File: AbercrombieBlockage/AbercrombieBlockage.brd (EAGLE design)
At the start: 56 x 51 mm, 30 parts, among them U1 CY8CKIT-142, U2 DMN3135LVT, U3 DMN3135LVT, U4 DMN3135LVT, U5 M95M01, U6 LDK130M-R

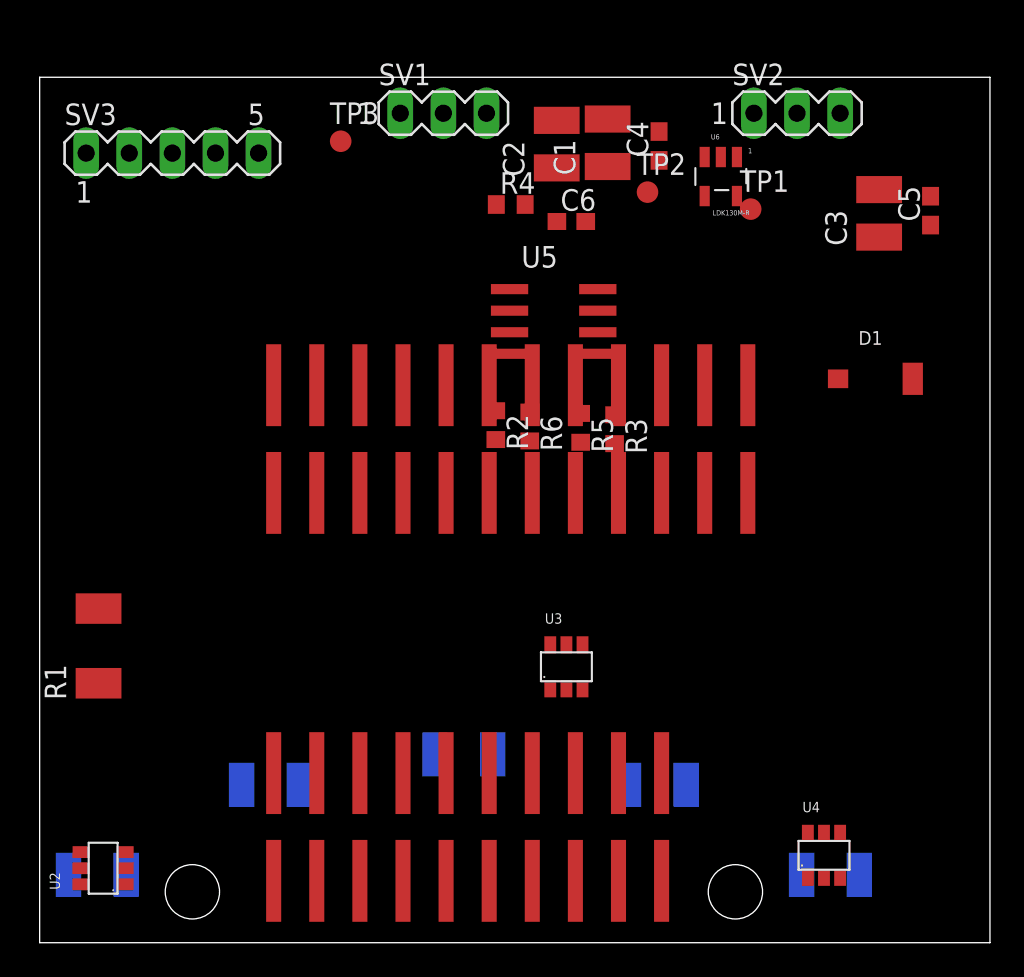
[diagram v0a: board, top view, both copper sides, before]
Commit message: Finished the schematic and placement. Starting routing for Abercrombie.
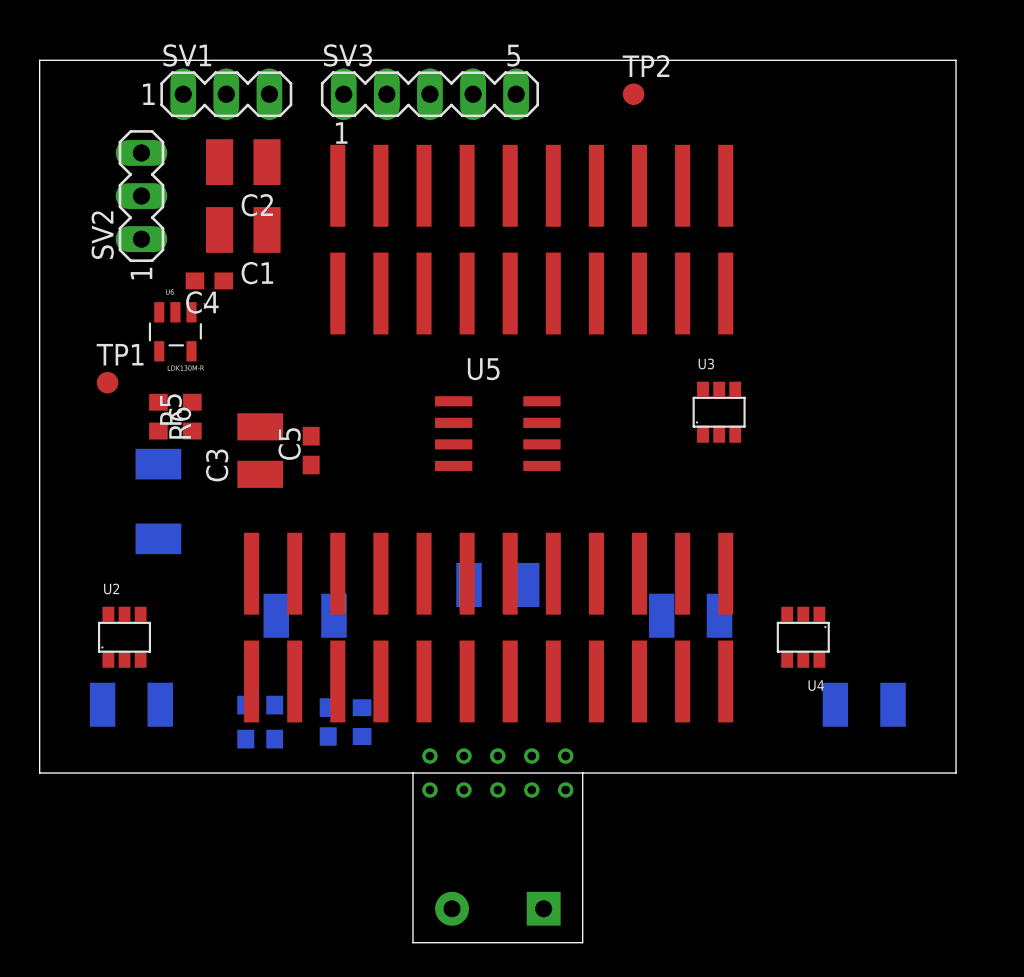
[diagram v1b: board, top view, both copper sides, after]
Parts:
- removed TP3: TPB1,27, testpad:B1,27
- D1: value BPW34 -> BPW34TH; device NicksParts:BPW34S -> NicksParts:BPW34
- moved TP1 39.3 mm to (4.00, 33.0)
- moved C5 39.1 mm to (16.0, 29.0)
- moved C3 39.1 mm to (13.0, 29.0)
- moved SV2 38.9 mm to (6.00, 44.0), turned to 90 degrees
- moved D1 38.3 mm to (27.0, 2.00), flipped to the bottom
- moved R4 34.8 mm to (13.0, 12.0), flipped to the bottom, turned to 180 degrees
- moved U6 33.4 mm to (8.00, 36.0)
- moved C6 32.8 mm to (17.0, 13.0), flipped to the bottom, turned to 90 degrees
- moved C4 27.7 mm to (10.0, 39.0), turned to 180 degrees
- moved R3 26.5 mm to (13.0, 14.0), flipped to the bottom, turned to 0 degrees
- moved R5 22.9 mm to (9.00, 31.0), turned to 90 degrees
- moved C1 22.1 mm to (12.0, 42.0), turned to 180 degrees
- moved R6 21.9 mm to (7.00, 31.0)
- moved R2 19.2 mm to (19.0, 13.0), flipped to the bottom
- moved C2 18.5 mm to (12.0, 46.0), turned to 180 degrees
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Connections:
- removed net N$11: C6.1, D1.C, R2.2, U1.P2.1
- removed net N$13: R3.2, R4.1, U1.P2.0
- removed net N$9: C6.2, R2.1, U1.P2.2
- new net OPAMP+: R3.2, R4.1, U1.2.0
- new net OPAMP-: C6.1, D1.C, R2.2, U1.2.1
- new net OPAMP_OUT: C6.2, R2.1, U1.2.2
- net CS: now also U1.1.5; no longer U1.P1.5
- net GND: now also U1.GND1
- net HOLD: now also U1.0.4; no longer U1.P0.4
- net LED1: now also U1.5.0; no longer U1.P3.6
- net LED2: now also U1.5.1; no longer U1.P3.4
- net LED3: now also U1.3.1; no longer U1.P3.2
- net LED4: now also U1.3.3; no longer U1.P3.0
- net LED5: now also U1.3.5; no longer U1.P4.0
- net MISO: now also U1.1.7; no longer U1.P1.6
- net MOSI: now also U1.0.0; no longer U1.P1.7
- net SCLK: now also U1.0.2; no longer U1.P1.3
- net SWDCLK: now also U1.0.7; no longer U1.P0.7
- net SWDIO: now also U1.0.6; no longer U1.P0.6
- net VREF: no longer U1.VREF
- net WP: now also U1.1.6; no longer U1.P1.4
- net XRES: no longer TP3.TP
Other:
- board size 56 x 51 mm -> 54 x 52 mm

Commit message: Fully routed Abercrombie design
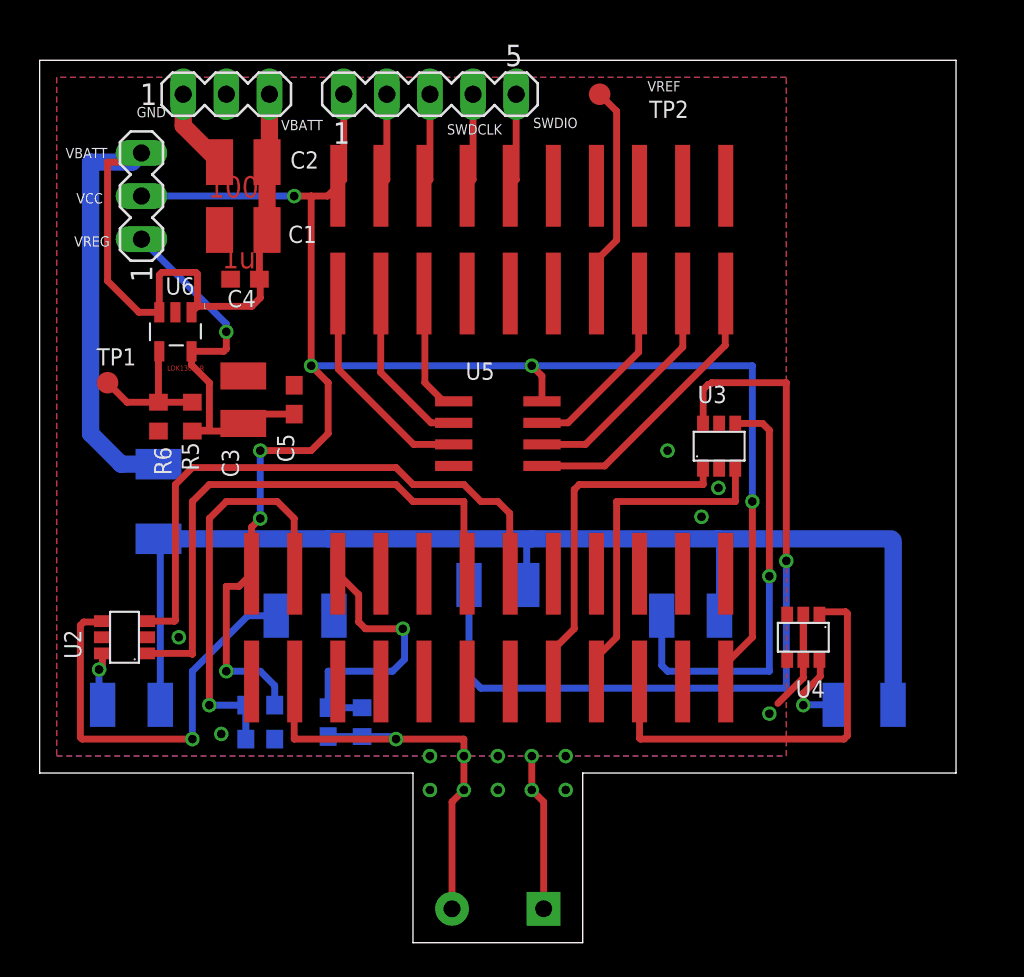
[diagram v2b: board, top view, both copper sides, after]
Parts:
- moved C3 3.16 mm to (12.0, 32.0)
- moved C5 3.16 mm to (15.0, 32.0)
- moved C4 2.10 mm to (12.1, 39.1)
- moved TP2 2.00 mm to (33.0, 50.0)
- moved U3 2.00 mm to (40.0, 29.3)
- turned U2 to 90 degrees
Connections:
- removed net VREF: TP2.TP
- new net N$9: TP2.TP, U1.VREF
- net LED1: now also U1.4.1; no longer U1.5.0
- net LED2: now also U1.4.0; no longer U1.5.1
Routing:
- net VCC: track 0.00 -> 102.4 mm, vias 0 -> 7
- net N$1: track 0.00 -> 74.9 mm
- net VBATT: track 0.00 -> 60.1 mm
- net N$4: track 0.00 -> 49.5 mm, vias 0 -> 1
- net LED2: track 0.00 -> 34.5 mm
- net LED1: track 0.00 -> 32.9 mm
- net GND: track 0.00 -> 28.1 mm, vias 0 -> 7
- net OPAMP-: track 0.00 -> 27.8 mm, vias 0 -> 1
- net N$5: track 0.00 -> 25.8 mm, vias 0 -> 1
- net N$3: track 0.00 -> 24.9 mm, vias 0 -> 1
- net LED5: track 0.00 -> 24.7 mm
- net OPAMP+: track 0.00 -> 24.2 mm, vias 0 -> 1
- net N$7: track 0.00 -> 23.2 mm, vias 0 -> 1
- net LED3: track 0.00 -> 20.5 mm
- net LED4: track 0.00 -> 20.1 mm
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- added copper zone on layer 1, net GND
- added copper zone on layer 16, net GND
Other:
- board text added: "GND"
- board text added: "SWDCLK"
- board text added: "SWDIO"
- board text added: "VBATT"
- board text added: "VCC"
- board text added: "VREF"
- board text added: "VREG"

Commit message: Minor update to the BLE connector
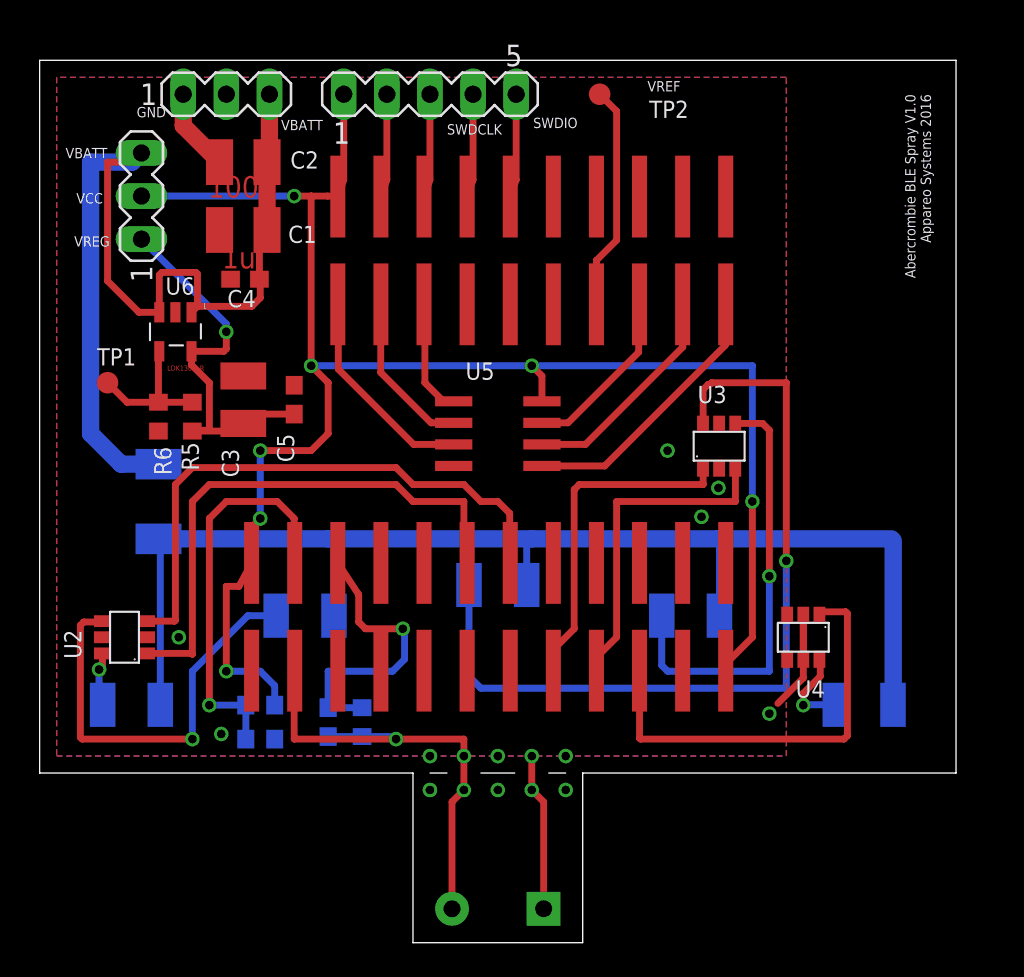
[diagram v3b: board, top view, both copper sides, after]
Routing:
- net N$9: track 12.7 -> 13.3 mm
- net LED5: track 24.7 -> 25.3 mm
- net LED3: track 20.5 -> 19.9 mm
- net LED4: track 20.1 -> 19.4 mm
- net OPAMP-: track 27.8 -> 28.4 mm
- net SCLK: track 13.8 -> 14.4 mm
- net MISO: track 10.2 -> 10.8 mm
- net OPAMP+: track 24.2 -> 24.8 mm
- net MOSI: track 16.8 -> 17.4 mm
- net WP: track 13.1 -> 13.7 mm
- net LED2: track 34.5 -> 35.1 mm
- net SWDIO: track 5.54 -> 6.09 mm
- net SWDCLK: track 5.54 -> 6.09 mm
- net XRES: track 5.54 -> 6.09 mm
- net GND: track 28.1 -> 28.7 mm
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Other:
- outline, holes or cut-outs redrawn
- board text added: "Abercrombie BLE Spray V1.0 Appareo Systems 2016"
